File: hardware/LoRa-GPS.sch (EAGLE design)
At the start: 34 parts, among them J2 MF-CON-MICROUSB-RIGHT, U1 MCP1703-3302E/CB, U2 MCP73831, Y1 CRYSTAL.ABS07

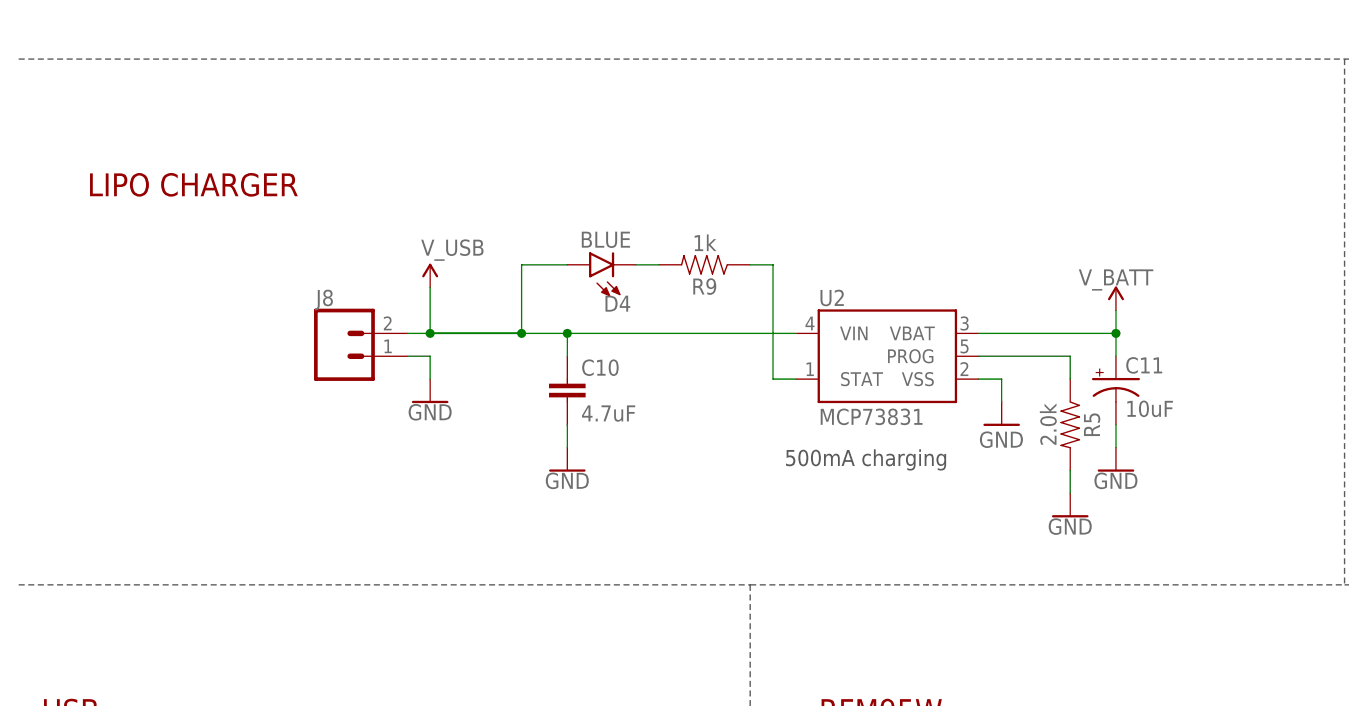
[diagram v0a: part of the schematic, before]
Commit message: remove DRC warnings
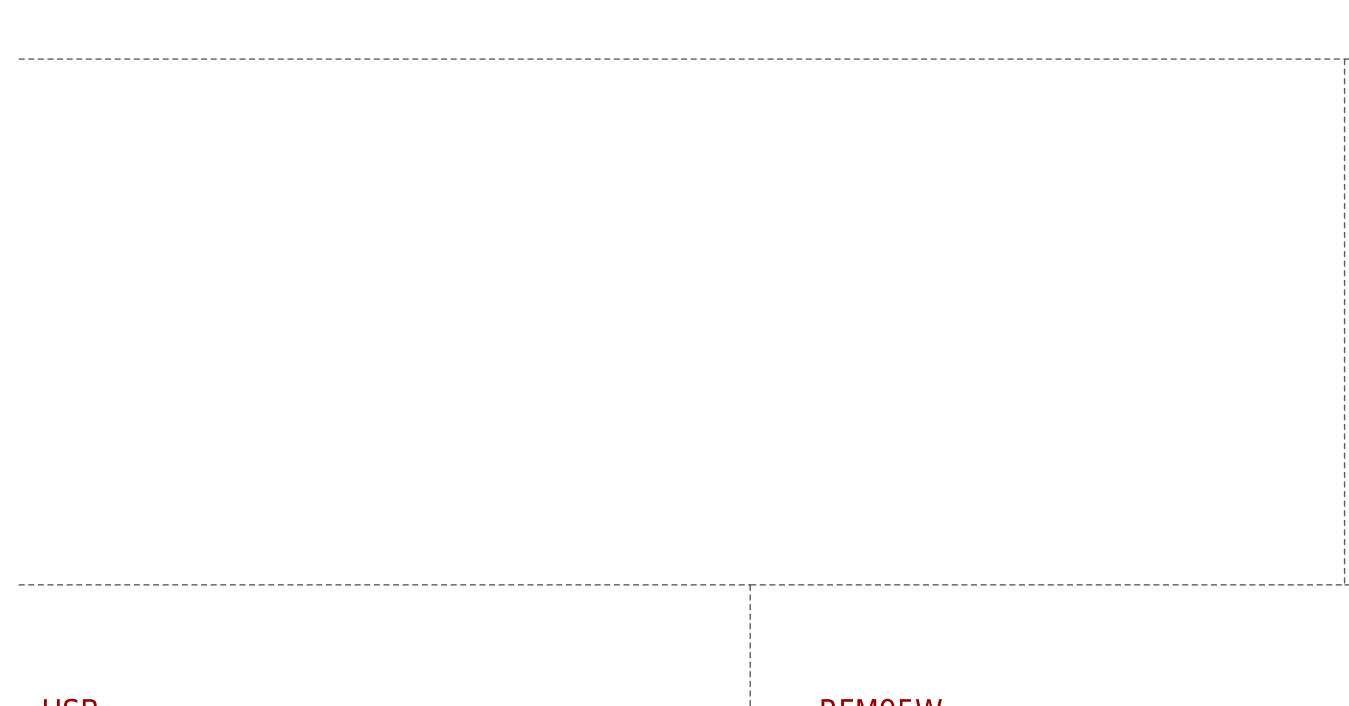
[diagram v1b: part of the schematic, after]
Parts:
- removed C10: 4.7uF, SparkFun-Capacitors:4.7UF-0603-6.3V-(10%)
- removed C11: 10uF, SparkFun-Capacitors:10UF-POLAR-EIA3216-16V-10%(TANT)
- removed D4: BLUE, SparkFun-LED:LED-BLUE0603
- removed J8: (no value), SparkFun-Connectors:CONN_021X02_NO_SILK
- removed R5: 2.0k, SparkFun-Resistors:2.0KOHM-0603-1/10W-5%
- removed R9: 1k, SparkFun-Resistors:1KOHM-0603-1/10W-1%
- removed U2: MCP73831, SparkFun-IC-Power:MCP73831
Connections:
- removed net CHARGE_STAT: R9.1, U2.STAT
- removed net N$11: R5.1, U2.PROG
- removed net N$8: D4.C, R9.2
- removed net V_BATT: C11.+, U2.VBAT
- removed net V_USB: C10.1, D4.A, J8.2, U2.VIN
- net GND: no longer C10.2, C11.-, J8.1, R5.2, U2.VSS
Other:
- note removed: "500mA charging"
- note removed: "LIPO CHARGER"
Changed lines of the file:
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@@
 <layer number="255" name="routoute" color="7" fill="1" visible="yes" active="yes"/>
 </layers>
-<schematic xreflabel="%F%N/%S.%C%R" xrefpart="/%S.%C%R">
+<schematic xreflabel="%F%N/%S" xrefpart="/%S.%C%R">
 <attributes>
 </attributes>
@@
 <part name="GND15" library="supply1" deviceset="GND" device=""/>
 <part name="FRAME2" library="frames" library_urn="urn:adsk.eagle:library:229" deviceset="FRAME_B_L" device=""/>
-<part name="C10" library="SparkFun-Capacitors" deviceset="4.7UF" device="-0603-6.3V-(10%)" value="4.7uF"/>
-<part name="GND18" library="SparkFun-PowerSymbols" deviceset="GND" device=""/>
-<part name="GND20" library="SparkFun-PowerSymbols" deviceset="GND" device=""/>
-<part name="D4" library="SparkFun-LED" deviceset="LED-BLUE" device="0603" value="BLUE"/>
-<part name="R9" library="SparkFun-Resistors" deviceset="1KOHM" device="-0603-1/10W-1%" value="1k"/>
-<part name="GND17" library="SparkFun-PowerSymbols" deviceset="GND" device=""/>
-<part name="U2" library="SparkFun-IC-Power" deviceset="MCP73831" device=""/>
-<part name="R5" library="SparkFun-Resistors" deviceset="2.0KOHM" device="-0603-1/10W-5%" value="2.0k"/>
-<part name="GND19" library="supply1" library_urn="urn:adsk.eagle:library:371" deviceset="GND" device=""/>
-<part name="GND21" library="SparkFun-PowerSymbols" deviceset="GND" device=""/>
-<part name="C11" library="SparkFun-Capacitors" deviceset="10UF-POLAR" device="-EIA3216-16V-10%(TANT)" value="10uF"/>
-<part name="J8" library="SparkFun-Connectors" deviceset="CONN_02" device="1X02_NO_SILK"/>
-<part name="SUPPLY4" library="SparkFun-PowerSymbols" deviceset="V_BATT" device=""/>
-<part name="SUPPLY5" library="SparkFun-PowerSymbols" deviceset="V_USB" device=""/>
 </parts>
 <sheets>
@@
 <text x="-187.96" y="-91.44" size="2.54" layer="94">RFM95W</text>
 <text x="-81.28" y="-91.44" size="2.54" layer="94">GPS</text>
-<text x="-191.77" y="-62.992" size="1.778" layer="97" font="vector">500mA charging</text>
-<text x="-269.24" y="-33.02" size="2.54" layer="94" font="vector">LIPO CHARGER</text>
 <wire x1="-276.86" y1="-76.2" x2="-195.58" y2="-76.2" width="0.1524" layer="97" style="shortdash"/>
 <wire x1="-195.58" y1="-76.2" x2="-129.54" y2="-76.2" width="0.1524" layer="97" style="shortdash"/>
@@
 <attribute name="DRAWING_NAME" x="60.96" y="-130.81" size="2.54" layer="94"/>
 </instance>
-<instance part="C10" gate="G$1" x="-215.9" y="-55.88" smashed="yes">
-<attribute name="NAME" x="-214.376" y="-52.959" size="1.778" layer="95" font="vector"/>
-<attribute name="VALUE" x="-214.376" y="-58.039" size="1.778" layer="96" font="vector"/>
-</instance>
-<instance part="GND18" gate="1" x="-215.9" y="-63.5" smashed="yes">
-<attribute name="VALUE" x="-215.9" y="-63.754" size="1.778" layer="96" align="top-center"/>
-</instance>
-<instance part="GND20" gate="1" x="-154.94" y="-63.5" smashed="yes">
-<attribute name="VALUE" x="-154.94" y="-63.754" size="1.778" layer="96" align="top-center"/>
-</instance>
-<instance part="D4" gate="G$1" x="-213.36" y="-40.64" smashed="yes" rot="R90">
-<attribute name="NAME" x="-208.788" y="-44.069" size="1.778" layer="95" font="vector" rot="R180"/>
-<attribute name="VALUE" x="-208.788" y="-38.735" size="1.778" layer="96" font="vector" rot="R180" align="top-left"/>
-</instance>
-<instance part="R9" gate="G$1" x="-200.66" y="-40.64" smashed="yes" rot="R180">
-<attribute name="NAME" x="-200.66" y="-42.164" size="1.778" layer="95" font="vector" rot="R180" align="bottom-center"/>
-<attribute name="VALUE" x="-200.66" y="-39.116" size="1.778" layer="96" font="vector" rot="R180" align="top-center"/>
-</instance>
-<instance part="GND17" gate="1" x="-231.14" y="-55.88" smashed="yes">
-<attribute name="VALUE" x="-231.14" y="-56.134" size="1.778" layer="96" align="top-center"/>
-</instance>
-<instance part="U2" gate="G$1" x="-180.34" y="-50.8" smashed="yes">
-<attribute name="NAME" x="-187.96" y="-45.212" size="1.778" layer="95"/>
-<attribute name="VALUE" x="-187.96" y="-58.42" size="1.778" layer="96"/>
-</instance>
-<instance part="R5" gate="G$1" x="-160.02" y="-58.42" smashed="yes" rot="R270">
-<attribute name="NAME" x="-158.496" y="-58.42" size="1.778" layer="95" font="vector" rot="R270" align="bottom-center"/>
-<attribute name="VALUE" x="-161.544" y="-58.42" size="1.778" layer="96" font="vector" rot="R270" align="top-center"/>
-</instance>
-<instance part="GND19" gate="1" x="-167.64" y="-58.42" smashed="yes">
-<attribute name="VALUE" x="-170.18" y="-60.96" size="1.778" layer="96"/>
-</instance>
-<instance part="GND21" gate="1" x="-160.02" y="-68.58" smashed="yes">
-<attribute name="VALUE" x="-160.02" y="-68.834" size="1.778" layer="96" align="top-center"/>
-</instance>
-<instance part="C11" gate="G$1" x="-154.94" y="-53.34" smashed="yes">
-<attribute name="NAME" x="-153.924" y="-52.705" size="1.778" layer="95" font="vector"/>
-<attribute name="VALUE" x="-153.924" y="-57.531" size="1.778" layer="96" font="vector"/>
-</instance>
-<instance part="J8" gate="G$1" x="-241.3" y="-50.8" smashed="yes">
-<attribute name="VALUE" x="-243.84" y="-55.626" size="1.778" layer="96" font="vector"/>
-<attribute name="NAME" x="-243.84" y="-45.212" size="1.778" layer="95" font="vector"/>
-</instance>
-<instance part="SUPPLY4" gate="G$1" x="-154.94" y="-45.72" smashed="yes">
-<attribute name="VALUE" x="-154.94" y="-42.926" size="1.778" layer="96" align="bottom-center"/>
-</instance>
-<instance part="SUPPLY5" gate="G$1" x="-231.14" y="-43.18" smashed="yes">
-<attribute name="VALUE" x="-232.156" y="-39.624" size="1.778" layer="96"/>
-</instance>
 </instances>
 <busses>
@@
 <pinref part="S2" gate="G$1" pin="1"/>
 <wire x1="-243.84" y1="17.78" x2="-243.84" y2="20.32" width="0.1524" layer="91"/>
-</segment>
-<segment>
-<wire x1="-215.9" y1="-58.42" x2="-215.9" y2="-60.96" width="0.1524" layer="91"/>
-<pinref part="C10" gate="G$1" pin="2"/>
-<pinref part="GND18" gate="1" pin="GND"/>
-</segment>
-<segment>
-<wire x1="-154.94" y1="-60.96" x2="-154.94" y2="-58.42" width="0.1524" layer="91"/>
-<pinref part="GND20" gate="1" pin="GND"/>
-<pinref part="C11" gate="G$1" pin="-"/>
-</segment>
-<segment>
-<wire x1="-233.68" y1="-50.8" x2="-231.14" y2="-50.8" width="0.1524" layer="91"/>
-<wire x1="-231.14" y1="-50.8" x2="-231.14" y2="-53.34" width="0.1524" layer="91"/>
-<pinref part="GND17" gate="1" pin="GND"/>
-<pinref part="J8" gate="G$1" pin="1"/>
-</segment>
-<segment>
-<wire x1="-170.18" y1="-53.34" x2="-167.64" y2="-53.34" width="0.1524" layer="91"/>
-<wire x1="-167.64" y1="-53.34" x2="-167.64" y2="-55.88" width="0.1524" layer="91"/>
-<pinref part="U2" gate="G$1" pin="VSS"/>
-<pinref part="GND19" gate="1" pin="GND"/>
-</segment>
-<segment>
-<wire x1="-160.02" y1="-66.04" x2="-160.02" y2="-63.5" width="0.1524" layer="91"/>
-<pinref part="R5" gate="G$1" pin="2"/>
-<pinref part="GND21" gate="1" pin="GND"/>
 </segment>
 </net>
@@
 </segment>
 </net>
-<net name="CHARGE_STAT" class="0">
-<segment>
-<wire x1="-190.5" y1="-53.34" x2="-193.04" y2="-53.34" width="0.1524" layer="91"/>
-<wire x1="-193.04" y1="-53.34" x2="-193.04" y2="-40.64" width="0.1524" layer="91"/>
-<wire x1="-193.04" y1="-40.64" x2="-195.58" y2="-40.64" width="0.1524" layer="91"/>
-<pinref part="U2" gate="G$1" pin="STAT"/>
-<pinref part="R9" gate="G$1" pin="1"/>
-</segment>
-</net>
-<net name="N$11" class="0">
-<segment>
-<wire x1="-170.18" y1="-50.8" x2="-160.02" y2="-50.8" width="0.1524" layer="91"/>
-<wire x1="-160.02" y1="-50.8" x2="-160.02" y2="-53.34" width="0.1524" layer="91"/>
-<pinref part="U2" gate="G$1" pin="PROG"/>
-<pinref part="R5" gate="G$1" pin="1"/>
-</segment>
-</net>
-<net name="N$8" class="0">
-<segment>
-<wire x1="-205.74" y1="-40.64" x2="-208.28" y2="-40.64" width="0.1524" layer="91"/>
-<pinref part="D4" gate="G$1" pin="C"/>
-<pinref part="R9" gate="G$1" pin="2"/>
-</segment>
-</net>
-<net name="V_USB" class="0">
-<segment>
-<wire x1="-233.68" y1="-48.26" x2="-220.98" y2="-48.26" width="0.1524" layer="91"/>
-<wire x1="-220.98" y1="-48.26" x2="-231.14" y2="-48.26" width="0.1524" layer="91"/>
-<wire x1="-231.14" y1="-48.26" x2="-215.9" y2="-48.26" width="0.1524" layer="91"/>
-<wire x1="-215.9" y1="-48.26" x2="-190.5" y2="-48.26" width="0.1524" layer="91"/>
-<wire x1="-215.9" y1="-50.8" x2="-215.9" y2="-48.26" width="0.1524" layer="91"/>
-<wire x1="-215.9" y1="-40.64" x2="-220.98" y2="-40.64" width="0.1524" layer="91"/>
-<wire x1="-220.98" y1="-40.64" x2="-220.98" y2="-48.26" width="0.1524" layer="91"/>
-<junction x="-215.9" y="-48.26"/>
-<junction x="-220.98" y="-48.26"/>
-<pinref part="U2" gate="G$1" pin="VIN"/>
-<pinref part="C10" gate="G$1" pin="1"/>
-<pinref part="D4" gate="G$1" pin="A"/>
-<pinref part="J8" gate="G$1" pin="2"/>
-<junction x="-231.14" y="-48.26"/>
-<pinref part="SUPPLY5" gate="G$1" pin="V_USB"/>
-<wire x1="-231.14" y1="-43.18" x2="-231.14" y2="-48.26" width="0.1524" layer="91"/>
-</segment>
-</net>
-<net name="V_BATT" class="0">
-<segment>
-<wire x1="-170.18" y1="-48.26" x2="-154.94" y2="-48.26" width="0.1524" layer="91"/>
-<wire x1="-154.94" y1="-50.8" x2="-154.94" y2="-48.26" width="0.1524" layer="91"/>
-<junction x="-154.94" y="-48.26"/>
-<pinref part="U2" gate="G$1" pin="VBAT"/>
-<pinref part="C11" gate="G$1" pin="+"/>
-<pinref part="SUPPLY4" gate="G$1" pin="V_BATT"/>
-<wire x1="-154.94" y1="-48.26" x2="-154.94" y2="-45.72" width="0.1524" layer="91"/>
-</segment>
-</net>

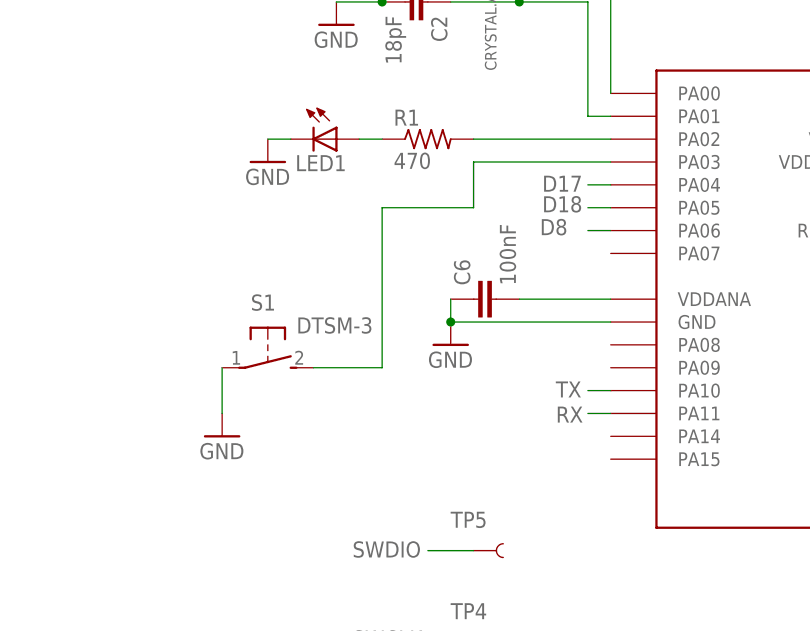
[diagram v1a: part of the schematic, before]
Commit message: remove switch move TP's
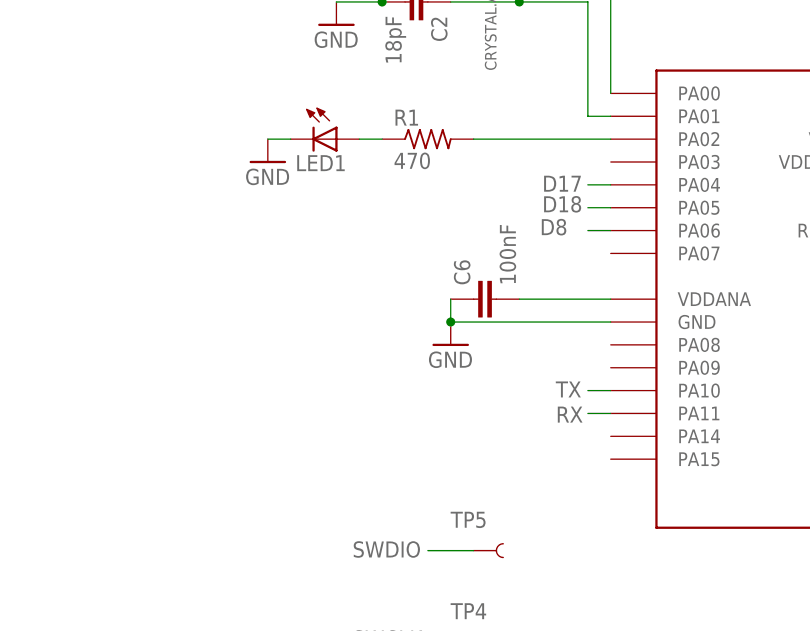
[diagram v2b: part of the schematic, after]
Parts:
- removed S1: DTSM-3, switch-tact:DTSM-3
- TP1: device SparkFun-Passives:TEST-POINTTP_15TH_THRU -> SparkFun-Passives:TEST-POINT3X5
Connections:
- removed net N$9: S1.2, SAMD21.PA03
- net GND: no longer S1.1
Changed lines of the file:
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@@
 <part name="GND16" library="supply1" deviceset="GND" device=""/>
 <part name="ANT" library="nootropicdesign" deviceset="M01" device=""/>
-<part name="S1" library="switch-tact" deviceset="DTSM-3" device=""/>
-<part name="GND3" library="supply1" deviceset="GND" device=""/>
-<part name="TP1" library="SparkFun-Passives" deviceset="TEST-POINT" device="TP_15TH_THRU" value="GND"/>
 <part name="TP5" library="SparkFun-Passives" deviceset="TEST-POINT" device="3X5" value=""/>
 <part name="TP4" library="SparkFun-Passives" deviceset="TEST-POINT" device="3X5" value=""/>
@@
 <part name="GND15" library="supply1" deviceset="GND" device=""/>
 <part name="FRAME2" library="frames" library_urn="urn:adsk.eagle:library:229" deviceset="FRAME_B_L" device=""/>
+<part name="TP1" library="SparkFun-Passives" deviceset="TEST-POINT" device="3X5" value="GND"/>
 </parts>
 <sheets>
@@
 <attribute name="NAME" x="-142.24" y="-99.822" size="1.778" layer="95" rot="R180"/>
 </instance>
-<instance part="S1" gate="G$1" x="-238.76" y="60.96" smashed="yes" rot="R270">
-<attribute name="NAME" x="-240.665" y="67.31" size="1.778" layer="95"/>
-<attribute name="VALUE" x="-235.585" y="64.77" size="1.778" layer="96"/>
-</instance>
-<instance part="GND3" gate="1" x="-243.84" y="53.34" smashed="yes">
-<attribute name="VALUE" x="-246.38" y="50.8" size="1.778" layer="96"/>
-</instance>
-<instance part="TP1" gate="G$1" x="-215.9" y="0" smashed="yes">
-<attribute name="NAME" x="-218.44" y="2.54" size="1.778" layer="95"/>
-<attribute name="VALUE" x="-218.44" y="-2.54" size="1.778" layer="96"/>
-</instance>
 <instance part="TP5" gate="G$1" x="-215.9" y="40.64" smashed="yes">
 <attribute name="NAME" x="-218.44" y="43.18" size="1.778" layer="95"/>
@@
 <attribute name="SHEET" x="129.54" y="-148.59" size="2.54" layer="94"/>
 <attribute name="DRAWING_NAME" x="60.96" y="-130.81" size="2.54" layer="94"/>
+</instance>
+<instance part="TP1" gate="G$1" x="-215.9" y="0" smashed="yes">
+<attribute name="NAME" x="-218.44" y="2.54" size="1.778" layer="95"/>
+<attribute name="VALUE" x="-218.44" y="-2.54" size="1.778" layer="96"/>
 </instance>
 </instances>
@@
 </segment>
 <segment>
-<pinref part="S1" gate="G$1" pin="1"/>
-<wire x1="-243.84" y1="60.96" x2="-243.84" y2="55.88" width="0.1524" layer="91"/>
-<pinref part="GND3" gate="1" pin="GND"/>
-</segment>
-<segment>
-<pinref part="TP1" gate="G$1" pin="1"/>
-<wire x1="-215.9" y1="0" x2="-223.52" y2="0" width="0.1524" layer="91"/>
-<pinref part="GND6" gate="1" pin="GND"/>
-</segment>
-<segment>
 <pinref part="GND15" gate="1" pin="GND"/>
 <pinref part="S2" gate="G$1" pin="1"/>
 <wire x1="-243.84" y1="17.78" x2="-243.84" y2="20.32" width="0.1524" layer="91"/>
+</segment>
+<segment>
+<pinref part="TP1" gate="G$1" pin="1"/>
+<pinref part="GND6" gate="1" pin="GND"/>
+<wire x1="-215.9" y1="0" x2="-223.52" y2="0" width="0.1524" layer="91"/>
 </segment>
 </net>
@@
 </segment>
 </net>
-<net name="N$9" class="0">
-<segment>
-<pinref part="S1" gate="G$1" pin="2"/>
-<wire x1="-233.68" y1="60.96" x2="-226.06" y2="60.96" width="0.1524" layer="91"/>
-<wire x1="-226.06" y1="60.96" x2="-226.06" y2="78.74" width="0.1524" layer="91"/>
-<wire x1="-226.06" y1="78.74" x2="-215.9" y2="78.74" width="0.1524" layer="91"/>
-<wire x1="-215.9" y1="78.74" x2="-215.9" y2="83.82" width="0.1524" layer="91"/>
-<pinref part="SAMD21" gate="G$1" pin="PA03"/>
-<wire x1="-215.9" y1="83.82" x2="-200.66" y2="83.82" width="0.1524" layer="91"/>
-</segment>
-</net>
